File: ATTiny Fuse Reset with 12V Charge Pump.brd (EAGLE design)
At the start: 38 parts, among them IC1 ATTinyx5/13, IC2 ATTinyx4, U2 ARDUINOR3-BPLACE

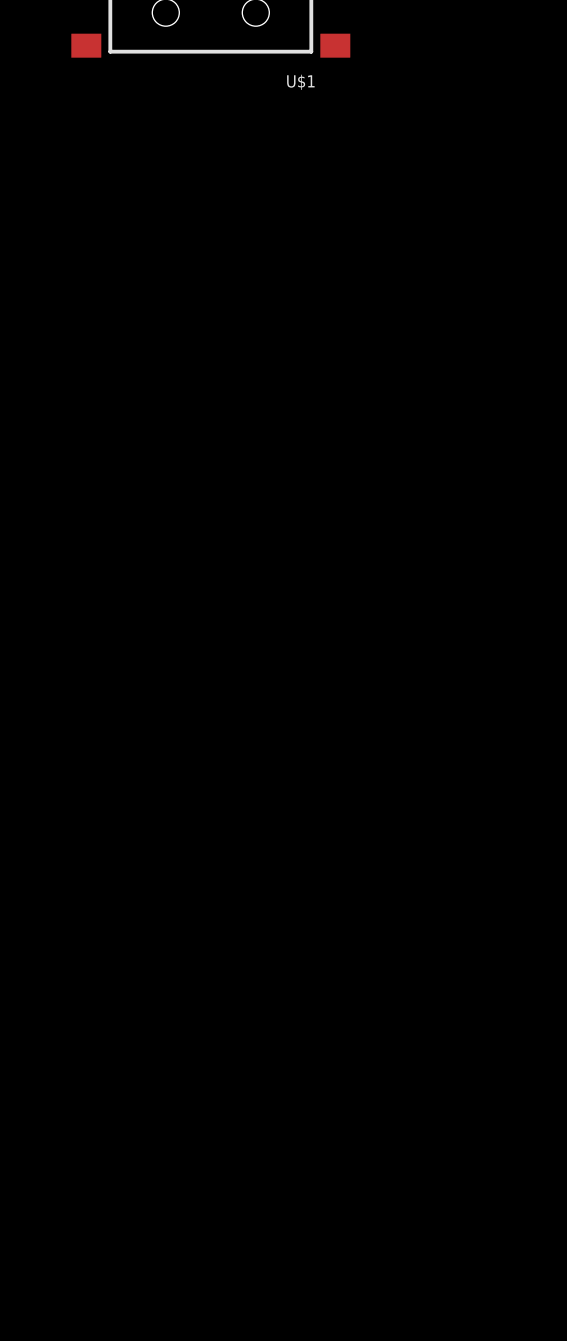
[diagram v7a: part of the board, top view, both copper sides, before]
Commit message: Added 3 LEDs. The LEDs indicate activity and error
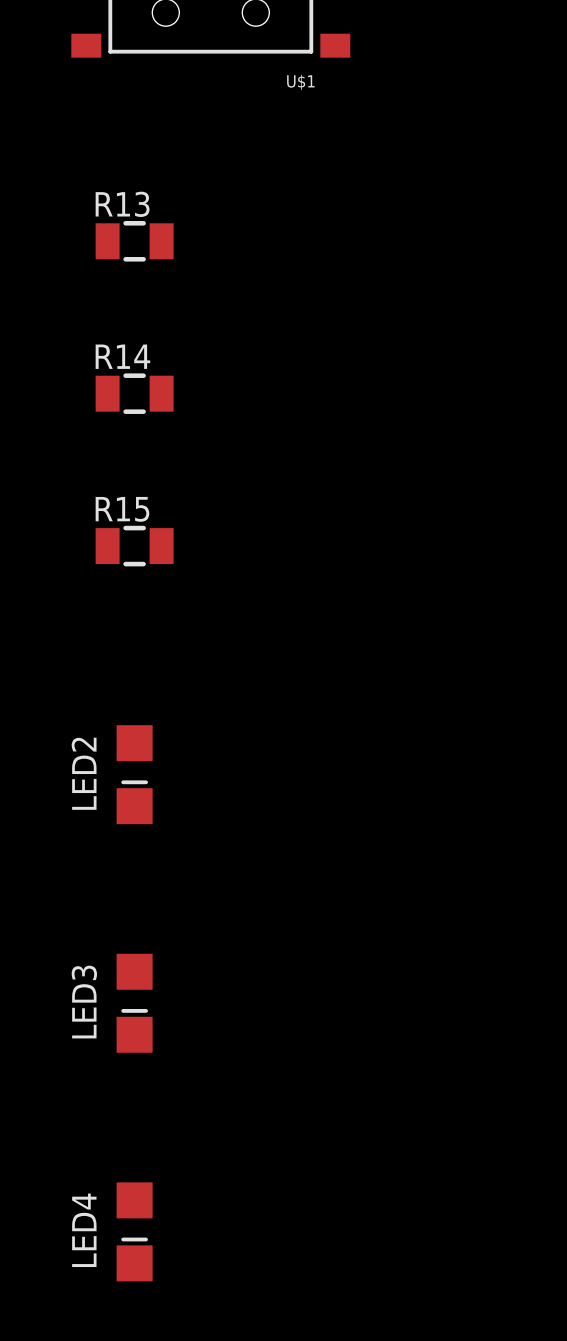
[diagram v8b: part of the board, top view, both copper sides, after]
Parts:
- added LED2: green, ATtami:LED-805
- added LED3: red, ATtami:LED-805
- added LED4: yellow, ATtami:LED-805
- added R13, R14, R15: 220R, ATtami:0805
- LED1: value (none) -> green
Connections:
- new net N$14: LED2.A, R13.1
- new net N$15: LED3.A, R14.1
- new net N$17: R14.2, U2.A3
- new net N$18: R13.2, U2.A2
- new net N$19: R15.1, U2.D6
- new net N$20: LED4.A, R15.2
- net 12V_OFF: now also R5.1; no longer R5.2
- net ATTINY_VCC: no longer LED1.A
- net GND: now also LED1.C, LED2.C, LED3.C, LED4.C; no longer R9.2
- net N$1: now also R5.2; no longer R5.1
- net N$4: now also LED1.A; no longer LED1.C
- net PUMP_VCC: now also R9.2
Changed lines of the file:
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@@
 <element name="U$6" library="ATtami" package="MOUNTINGHOLE_2.0_PLATED" value="MOUNTINGHOLE2.0" x="38.1" y="35.56"/>
 <element name="R9" library="ATtami" package="0805" value="220R" x="43.18" y="39.37" rot="R90"/>
-<element name="LED1" library="ATtami" package="LED-805" value="" x="30.48" y="27.94" rot="R270"/>
+<element name="LED1" library="ATtami" package="LED-805" value="green" x="30.48" y="27.94" rot="R270"/>
 <element name="R10" library="ATtami" package="0805" value="1k" x="27.94" y="25.4" rot="R180"/>
 <element name="D5" library="ATtami" package="SOD-323" value="1N4148" x="25.4" y="27.94" rot="R270"/>
@@
 <element name="C6" library="ATtami" package="0805" value="2uF" x="2.54" y="-15.24"/>
 <element name="U$1" library="SparkFun-Electromechanical" package="KPS-1290" value="SWITCH_SPDT" x="5.08" y="-22.86"/>
+<element name="R13" library="ATtami" package="0805" value="220R" x="2.54" y="-30.48"/>
+<element name="R14" library="ATtami" package="0805" value="220R" x="2.54" y="-35.56"/>
+<element name="R15" library="ATtami" package="0805" value="220R" x="2.54" y="-40.64"/>
+<element name="LED2" library="ATtami" package="LED-805" value="green" x="2.54" y="-48.26"/>
+<element name="LED3" library="ATtami" package="LED-805" value="red" x="2.54" y="-55.88"/>
+<element name="LED4" library="ATtami" package="LED-805" value="yellow" x="2.54" y="-63.5"/>
 </elements>
 <signals>
@@
 <contactref element="C4" pad="2"/>
 <contactref element="T1" pad="3"/>
-<contactref element="R8" pad="1"/>
 <contactref element="IC1" pad="4"/>
-<contactref element="R9" pad="2"/>
-<contactref element="ZD1" pad="A"/>
 <contactref element="JP11" pad="6"/>
 <contactref element="U2" pad="GND2"/>
@@
 <contactref element="-HEADERS3" pad="10"/>
 <contactref element="-HEADERS2" pad="10"/>
+<contactref element="LED4" pad="C"/>
+<contactref element="LED1" pad="C"/>
+<contactref element="LED2" pad="C"/>
+<contactref element="LED3" pad="C"/>
+<contactref element="R8" pad="1"/>
+<contactref element="ZD1" pad="A"/>
 <wire x1="46.99" y1="36.83" x2="57.15" y2="36.83" width="0" layer="19" extent="1-1"/>
 <wire x1="46.99" y1="40.81" x2="46.99" y2="36.83" width="0" layer="19" extent="1-1"/>
-<wire x1="43.18" y1="40.27" x2="46.99" y2="40.81" width="0" layer="19" extent="1-1"/>
-<wire x1="40.64" y1="40.27" x2="43.18" y2="40.27" width="0" layer="19" extent="1-1"/>
+<wire x1="40.64" y1="40.27" x2="46.99" y2="40.81" width="0" layer="19" extent="1-1"/>
 <wire x1="35.56" y1="44.08" x2="40.64" y2="40.27" width="0" layer="19" extent="1-1"/>
 <wire x1="62.595" y1="27.94" x2="57.15" y2="36.83" width="0" layer="19" extent="1-1"/>
@@
 <wire x1="11.43" y1="35.56" x2="11.43" y2="38.1" width="0" layer="19" extent="1-1"/>
 <wire x1="11.43" y1="33.02" x2="11.43" y2="35.56" width="0" layer="19" extent="1-1"/>
-<wire x1="58.42" y1="8.89" x2="62.595" y2="27.94" width="0" layer="19" extent="1-1"/>
-<wire x1="48.26" y1="8.89" x2="58.42" y2="8.89" width="0" layer="19" extent="1-1"/>
-<wire x1="45.72" y1="8.89" x2="48.26" y2="8.89" width="0" layer="19" extent="1-1"/>
-<wire x1="43.18" y1="8.89" x2="45.72" y2="8.89" width="0" layer="19" extent="1-1"/>
-<wire x1="40.64" y1="8.89" x2="43.18" y2="8.89" width="0" layer="19" extent="1-1"/>
-<wire x1="43.18" y1="2.54" x2="43.18" y2="8.89" width="0" layer="19" extent="1-1"/>
-<wire x1="40.64" y1="2.54" x2="43.18" y2="2.54" width="0" layer="19" extent="1-1"/>
-<wire x1="21.59" y1="1.27" x2="40.64" y2="2.54" width="0" layer="19" extent="1-1"/>
-<wire x1="21.59" y1="11.43" x2="21.59" y2="1.27" width="0" layer="19" extent="1-1"/>
+<wire x1="31.53" y1="27.94" x2="25.4" y2="40.64" width="0" layer="19" extent="1-1"/>
+<wire x1="21.59" y1="11.43" x2="31.53" y2="27.94" width="0" layer="19" extent="1-1"/>
+<wire x1="21.59" y1="1.27" x2="21.59" y2="11.43" width="0" layer="19" extent="1-1"/>
 <wire x1="3.81" y1="11.43" x2="21.59" y2="11.43" width="0" layer="19" extent="1-1"/>
 <wire x1="3.44" y1="-5.08" x2="3.81" y2="11.43" width="0" layer="19" extent="1-1"/>
 <wire x1="3.44" y1="-15.24" x2="3.44" y2="-5.08" width="0" layer="19" extent="1-1"/>
+<wire x1="40.64" y1="2.54" x2="21.59" y2="1.27" width="0" layer="19" extent="1-1"/>
+<wire x1="43.18" y1="2.54" x2="40.64" y2="2.54" width="0" layer="19" extent="1-1"/>
+<wire x1="43.18" y1="8.89" x2="43.18" y2="2.54" width="0" layer="19" extent="1-1"/>
+<wire x1="45.72" y1="8.89" x2="43.18" y2="8.89" width="0" layer="19" extent="1-1"/>
+<wire x1="48.26" y1="8.89" x2="45.72" y2="8.89" width="0" layer="19" extent="1-1"/>
+<wire x1="40.64" y1="8.89" x2="43.18" y2="8.89" width="0" layer="19" extent="1-1"/>
+<wire x1="58.42" y1="8.89" x2="48.26" y2="8.89" width="0" layer="19" extent="1-1"/>
+<wire x1="2.54" y1="-47.21" x2="3.44" y2="-15.24" width="0" layer="19" extent="1-1"/>
+<wire x1="2.54" y1="-54.83" x2="2.54" y2="-47.21" width="0" layer="19" extent="1-1"/>
+<wire x1="2.54" y1="-62.45" x2="2.54" y2="-54.83" width="0" layer="19" extent="1-1"/>
 </signal>
 <signal name="VIN">
@@
 <contactref element="IC1" pad="8"/>
 <contactref element="C6" pad="1"/>
-<contactref element="LED1" pad="A"/>
 <contactref element="R10" pad="1"/>
 <contactref element="-HEADERS1" pad="9"/>
@@
 <contactref element="-HEADERS2" pad="9"/>
 <wire x1="54.61" y1="36.83" x2="41.656" y2="50.8" width="0" layer="19" extent="1-1"/>
-<wire x1="29.43" y1="27.94" x2="41.656" y2="50.8" width="0" layer="19" extent="1-1"/>
-<wire x1="28.84" y1="25.4" x2="29.43" y2="27.94" width="0" layer="19" extent="1-1"/>
-<wire x1="17.78" y1="33.02" x2="29.43" y2="27.94" width="0" layer="19" extent="1-1"/>
+<wire x1="28.84" y1="25.4" x2="54.61" y2="36.83" width="0" layer="19" extent="1-1"/>
+<wire x1="17.78" y1="33.02" x2="28.84" y2="25.4" width="0" layer="19" extent="1-1"/>
 <wire x1="3.81" y1="40.64" x2="17.78" y2="33.02" width="0" layer="19" extent="1-1"/>
 <wire x1="21.59" y1="3.81" x2="28.84" y2="25.4" width="0" layer="19" extent="1-1"/>
@@
 <contactref element="U2" pad="D4"/>
 <contactref element="D1" pad="AQ"/>
+<contactref element="R9" pad="2"/>
 <wire x1="52.07" y1="44.069" x2="53.34" y2="50.8" width="0" layer="19" extent="1-1"/>
-</signal>
-<signal name="N$4">
-<contactref element="R9" pad="1"/>
-<contactref element="LED1" pad="C"/>
-<wire x1="31.53" y1="27.94" x2="43.18" y2="38.47" width="0" layer="19" extent="1-1"/>
+<wire x1="43.18" y1="40.27" x2="52.07" y2="44.069" width="0" layer="19" extent="1-1"/>
 </signal>
 <signal name="N$6">
@@
 </signal>
 <signal name="12V_OFF">
-<contactref element="R5" pad="2"/>
 <contactref element="U2" pad="D5"/>
-<wire x1="48.26" y1="47.89" x2="50.8" y2="50.8" width="0" layer="19" extent="1-1"/>
+<contactref element="R5" pad="1"/>
+<wire x1="48.26" y1="46.09" x2="50.8" y2="50.8" width="0" layer="19" extent="1-1"/>
 </signal>
 <signal name="N$1">
-<contactref element="R5" pad="1"/>
 <contactref element="T1" pad="1"/>
 <contactref element="R11" pad="1"/>
-<wire x1="47.94" y1="43.01" x2="48.26" y2="46.09" width="0" layer="19" extent="1-1"/>
+<contactref element="R5" pad="2"/>
+<wire x1="47.94" y1="43.01" x2="48.26" y2="47.89" width="0" layer="19" extent="1-1"/>
 <wire x1="1.64" y1="-5.08" x2="47.94" y2="43.01" width="0" layer="19" extent="1-1"/>
 </signal>
@@
 <wire x1="7.33" y1="-20.61" x2="50.8" y2="8.89" width="0" layer="19" extent="1-1"/>
 </signal>
+<signal name="N$14">
+<contactref element="R13" pad="1"/>
+<contactref element="LED2" pad="A"/>
+<wire x1="1.64" y1="-30.48" x2="2.54" y2="-49.31" width="0" layer="19" extent="1-1"/>
+</signal>
+<signal name="N$15">
+<contactref element="R14" pad="1"/>
+<contactref element="LED3" pad="A"/>
+<wire x1="1.64" y1="-35.56" x2="2.54" y2="-56.93" width="0" layer="19" extent="1-1"/>
+</signal>
+<signal name="N$17">
+<contactref element="R14" pad="2"/>
+<contactref element="U2" pad="A3"/>
+<wire x1="3.44" y1="-35.56" x2="58.42" y2="2.54" width="0" layer="19" extent="1-1"/>
+</signal>
+<signal name="N$18">
+<contactref element="R13" pad="2"/>
+<contactref element="U2" pad="A2"/>
+<wire x1="3.44" y1="-30.48" x2="55.88" y2="2.54" width="0" layer="19" extent="1-1"/>
+</signal>
+<signal name="N$19">
+<contactref element="U2" pad="D6"/>
+<contactref element="R15" pad="1"/>
+<wire x1="1.64" y1="-40.64" x2="48.26" y2="50.8" width="0" layer="19" extent="1-1"/>
+</signal>
+<signal name="N$20">
+<contactref element="R15" pad="2"/>
+<contactref element="LED4" pad="A"/>
+<wire x1="3.44" y1="-40.64" x2="2.54" y2="-64.55" width="0" layer="19" extent="1-1"/>
+</signal>
+<signal name="N$4">
+<contactref element="R9" pad="1"/>
+<contactref element="LED1" pad="A"/>
+<wire x1="29.43" y1="27.94" x2="43.18" y2="38.47" width="0" layer="19" extent="1-1"/>
+</signal>
 </signals>
